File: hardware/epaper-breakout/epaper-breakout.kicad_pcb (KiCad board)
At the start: 2 copper layers, 88 x 67 mm, 107 parts, among them J1 USB_C_16P, J2 Conn_02x06_Counter_Clockwise, Q1 AO3401A, Q2 MMBT3904, Q3 MMBT3904, Q4 MMBT3904, Q5 2N7002, Q6 AO3401A, Q7 AO3401A, SW1 SW_DIP_x01, U1 LT1945, U10 ESP32-WROVER, U11 PCF8563T, U12 MCP9700AT-ETT, U13 ED060XC5, U14 FPC-TOUCH, U2 LT1945, U3 XC6206PxxxMR, U4 CH340C, U5 74HC4094-normal, U6 LM358, U7 CONN-Battery, U8 TP4056, U9 MCP1700-3302E_SOT23, Y1 Crystal

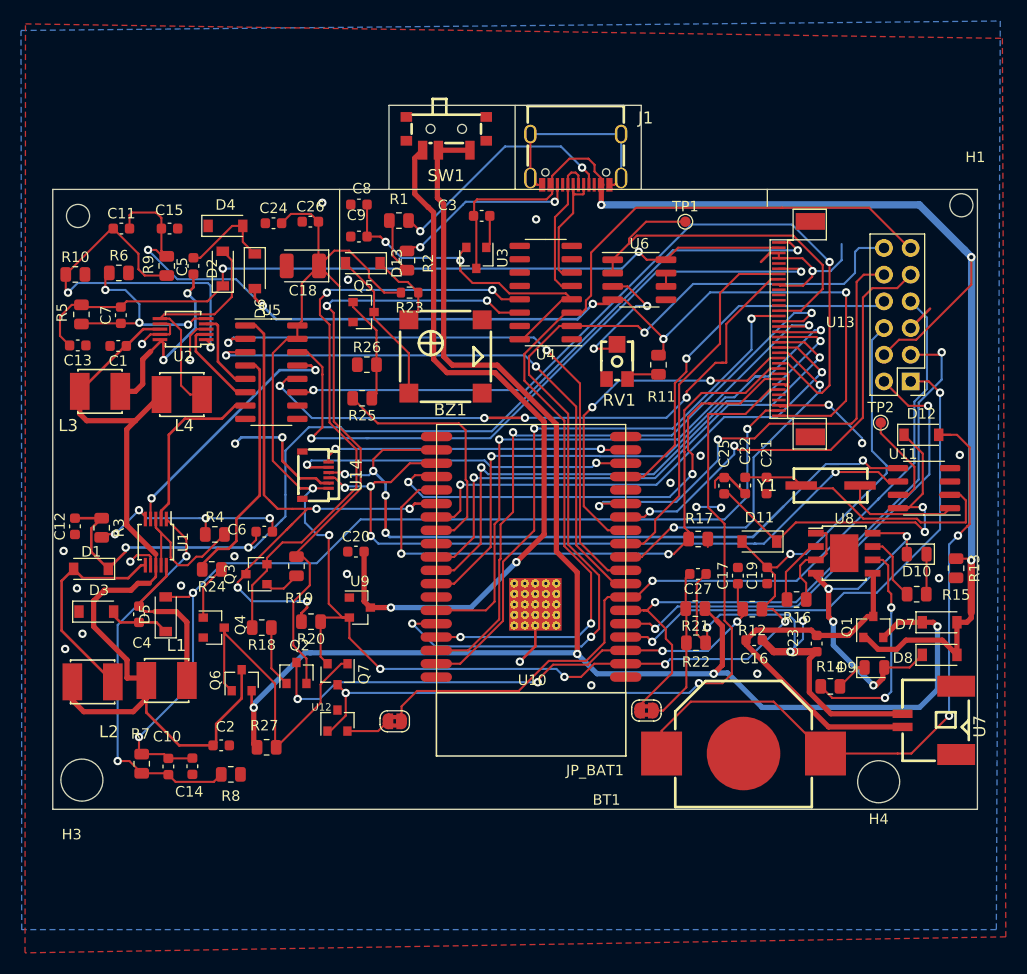
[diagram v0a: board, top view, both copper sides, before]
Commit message: change i2c bus pin
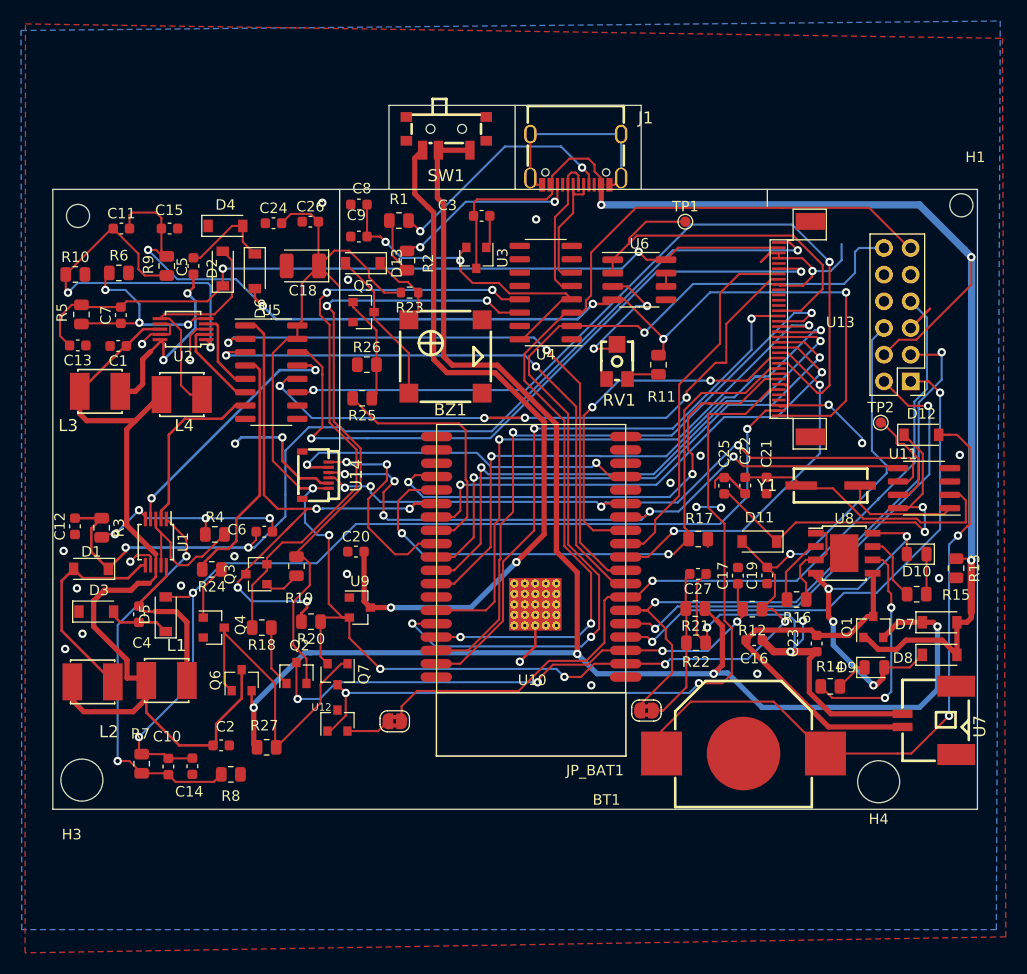
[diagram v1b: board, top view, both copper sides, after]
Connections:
- J1 pad A8: (no net) -> Net-(J1-PadA8)
- J1 pad B8: (no net) -> Net-(J1-PadB8)
- J2 pad 10: /MISO -> Net-(J2-Pad10)
- J2 pad 8: /MOSI -> Net-(J2-Pad8)
- J2 pad 9: /SCLK -> Net-(J2-Pad9)
- U10 pad 13: /SCLK -> /TCH_SDA
- U10 pad 14: /MISO -> /TCH_SCL
- U10 pad 16: /MOSI -> /TCH_INT
- U10 pad 17: /TCH_INT -> Net-(U10-Pad17)
- U10 pad 18: /TCH_RST -> Net-(U10-Pad18)
- U10 pad 19: (no net) -> Net-(U10-Pad19)
- U10 pad 20: (no net) -> Net-(U10-Pad20)
- U10 pad 21: /TCH_SDA -> Net-(U10-Pad21)
- U10 pad 22: /TCH_SCL -> Net-(U10-Pad22)
- U10 pad 28: (no net) -> /TCH_RST
- U10 pad 32: (no net) -> Net-(U10-Pad32)
- U11 pad 3: (no net) -> Net-(U11-Pad3)
- U13 pad 22: (no net) -> Net-(U13-Pad22)
- U13 pad 23: (no net) -> Net-(U13-Pad23)
- U13 pad 24: (no net) -> Net-(U13-Pad24)
- U13 pad 25: (no net) -> Net-(U13-Pad25)
- U13 pad 30: (no net) -> Net-(U13-Pad30)
- U13 pad 4: (no net) -> Net-(U13-Pad4)
- U13 pad 5: (no net) -> Net-(U13-Pad5)
- U4 pad 10: (no net) -> Net-(U4-Pad10)
- U4 pad 11: (no net) -> Net-(U4-Pad11)
- U4 pad 12: (no net) -> Net-(U4-Pad12)
- U4 pad 15: (no net) -> Net-(U4-Pad15)
- U4 pad 7: (no net) -> Net-(U4-Pad7)
- U4 pad 8: (no net) -> Net-(U4-Pad8)
- U4 pad 9: (no net) -> Net-(U4-Pad9)
- U5 pad 10: (no net) -> Net-(U5-Pad10)
- U5 pad 9: (no net) -> Net-(U5-Pad9)
- U8 pad 9: (no net) -> Net-(U8-Pad9)
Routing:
- net /MISO: track 47.7 -> 0.00 mm, vias 2 -> 0
- net /SCLK: track 44.2 -> 0.00 mm, vias 2 -> 0
- net /MOSI: track 35.7 -> 0.00 mm, vias 1 -> 0
- net /TCH_RST: track 29.6 -> 20.3 mm
- net /TCH_SDA: track 71.9 -> 65.0 mm
- net /TCH_SCL: track 72.2 -> 66.3 mm
- net /TCH_INT: track 33.3 -> 34.5 mm
- net /EP_STH: track 34.6 -> 35.5 mm
- net Net-(TP2-Pad1): track 9.41 -> 10.2 mm
- net Net-(J2-Pad8): track 0.00 -> 0.63 mm

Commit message: change usb-c type
2022-08-27
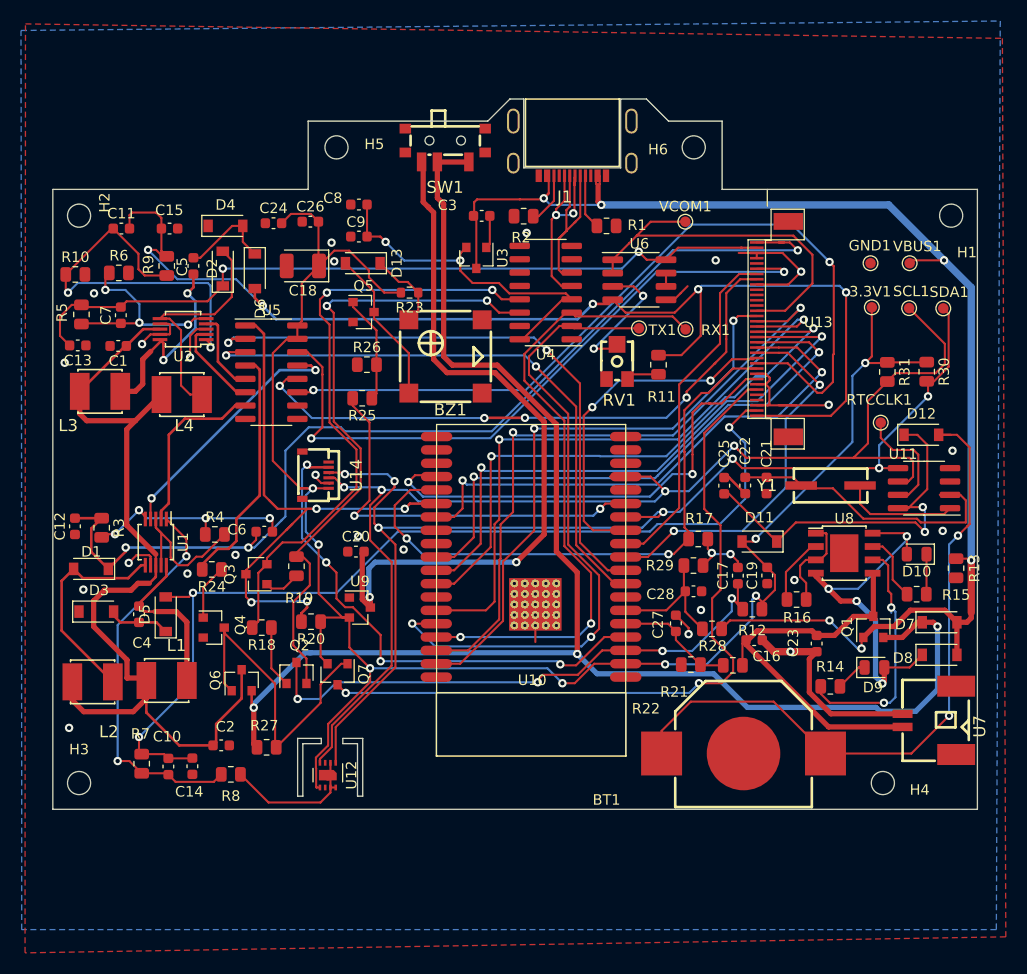
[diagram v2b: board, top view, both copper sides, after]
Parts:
- removed J2: Conn_02x06_Counter_Clockwise, Connector_PinHeader_2.54mm:PinHeader_2x06_P2.54mm_Vertical
- removed JP_BAT1, JP_TEMP1: Jumper, Jumper:SolderJumper-2_P1.3mm_Bridged2Bar_RoundedPad1.0x1.5mm
- added 3.3V1: TestPoint_Probe, TestPoint:TestPoint_Pad_D1.0mm, F.Cu at (101.0, 42.2)
- added C28: 0.1uF, Capacitor_SMD:C_0603_1608Metric, F.Cu at (84.0, 69.2)
- added GND1: TestPoint_Probe, TestPoint:TestPoint_Pad_D1.0mm, F.Cu at (100.8, 38.0)
- added H5: MountingHole, MountingHole:MountingHole_2.2mm_M2, F.Cu at (50.0, 27.0)
- added H6: MountingHole, MountingHole:MountingHole_2.2mm_M2, F.Cu at (84.0, 27.0)
- added R28: 680k, Resistor_SMD:R_0805_2012Metric, F.Cu at (85.7, 72.8)
- added R29: 150k, Resistor_SMD:R_0805_2012Metric, F.Cu at (84.0, 66.8)
- added R30: 10k, Resistor_SMD:R_0805_2012Metric, F.Cu at (106.2, 48.4)
- added R31: 10k, Resistor_SMD:R_0805_2012Metric, F.Cu at (102.4, 48.4)
- added RX1: TestPoint_Probe, TestPoint:TestPoint_Pad_D1.0mm, F.Cu at (83.2, 44.3)
- added SCL1: TestPoint_Probe, TestPoint:TestPoint_Pad_D1.0mm, F.Cu at (104.5, 42.3)
- added SDA1: TestPoint_Probe, TestPoint:TestPoint_Pad_D1.0mm, F.Cu at (107.8, 42.3)
- added TX1: TestPoint_Probe, TestPoint:TestPoint_Pad_D1.0mm, F.Cu at (78.8, 44.2)
- added VBUS1: TestPoint_Probe, TestPoint:TestPoint_Pad_D1.0mm, F.Cu at (104.5, 38.0)
- H3, H4: footprint MountingHole:MountingHole_4mm -> MountingHole:MountingHole_2.2mm_M2
- J1: footprint epaper-breakout:JLC_USB-C-SMD_KH-TYPE-C-16P -> epaper-breakout:JLC_USB-C-SMD_TYPE-C-31-M-13C
- U12: value MCP9700AT-ETT -> GHT30_DIS; footprint Package_TO_SOT_SMD:SOT-23 -> Sensor_Humidity:Sensirion_DFN-8-1EP_2.5x2.5mm_P0.5mm_EP1.1x1.7mm
- moved R1 19.8 mm to (75.7, 34.5), turned to 0 degrees
- moved R2 11.9 mm to (67.8, 33.5), turned to 180 degrees
- moved R21 6.48 mm to (87.7, 76.3)
- moved U12 5.28 mm to (49.2, 86.8), turned to 270 degrees
- moved C27 5.15 mm to (82.3, 72.3), turned to 270 degrees
- moved R22 2.13 mm to (83.7, 76.2), turned to 180 degrees
- moved U13 2.10 mm to (90.0, 44.3)
- moved H1 1.39 mm to (108.5, 33.5)
- moved SW1 1.12 mm to (60.4, 26.8)
- moved J1 1.10 mm to (72.5, 27.1)
- moved H4 0.42 mm to (102.0, 87.5)
- moved H3 0.39 mm to (25.5, 87.5)
- moved H2 0.10 mm to (25.5, 33.5), turned to 180 degrees
- renumbered TP2 to RTCCLK1, TP1 to VCOM1
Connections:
- C27 pad 2: Net-(C27-Pad2) -> /SENSOR_BAT
- R21 pad 1: VIN -> BAT+
- R21 pad 2: Net-(C27-Pad2) -> /SENSOR_BAT
- R22 pad 1: Net-(C27-Pad2) -> /SENSOR_BAT
- U10 pad 14: /TCH_SCL -> /BUZZER
- U10 pad 16: /TCH_INT -> /TCH_SCL
- U10 pad 27: /BUZZER -> Net-(U10-Pad27)
- U10 pad 28: /TCH_RST -> Net-(U10-Pad28)
- U10 pad 4: /SENSOR_VP -> /TCH_INT
- U10 pad 5: /SENSOR_VN -> /SENSOR_BAT
- U10 pad 6: /A0 -> /SENSOR_VBUS
- U10 pad 7: /A1 -> Net-(U10-Pad7)
- U12 pad 1: EPD_VDD -> /TCH_SDA
- U12 pad 2: Net-(JP_TEMP1-Pad1) -> GND
- U12 pad 3: GND -> Net-(U12-Pad3)
- U14 pad 6: /TCH_RST -> Net-(U14-Pad6)
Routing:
- net /A1: track 78.9 -> 0.00 mm, vias 1 -> 0
- net /A0: track 61.4 -> 0.00 mm, vias 2 -> 0
- net /TCH_SCL: track 66.3 -> 120.9 mm
- net /SENSOR_VP: track 50.9 -> 0.00 mm, vias 2 -> 0
- net GND: track 168.1 -> 119.4 mm, vias 30 -> 26
- net /TCH_SDA: track 65.0 -> 112.5 mm, vias 5 -> 7
- net /SENSOR_VN: track 46.9 -> 0.00 mm, vias 2 -> 0
- net /USB_RXD: track 91.5 -> 62.1 mm
- net /USB_TXD: track 90.2 -> 62.1 mm, vias 3 -> 2
- net /TCH_RST: track 20.3 -> 0.00 mm, vias 2 -> 0
- net Net-(J1-PadA5): track 23.0 -> 5.25 mm, vias 2 -> 0
- net Net-(C27-Pad2): track 15.0 -> 0.00 mm
- net /TCH_INT: track 34.5 -> 49.5 mm, vias 2 -> 4
- net /BUZZER: track 23.8 -> 38.7 mm, vias 0 -> 2
- net /+3.3V: track 161.1 -> 174.5 mm, vias 7 -> 8
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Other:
- board size 88 x 67 mm -> 88 x 67.6 mm

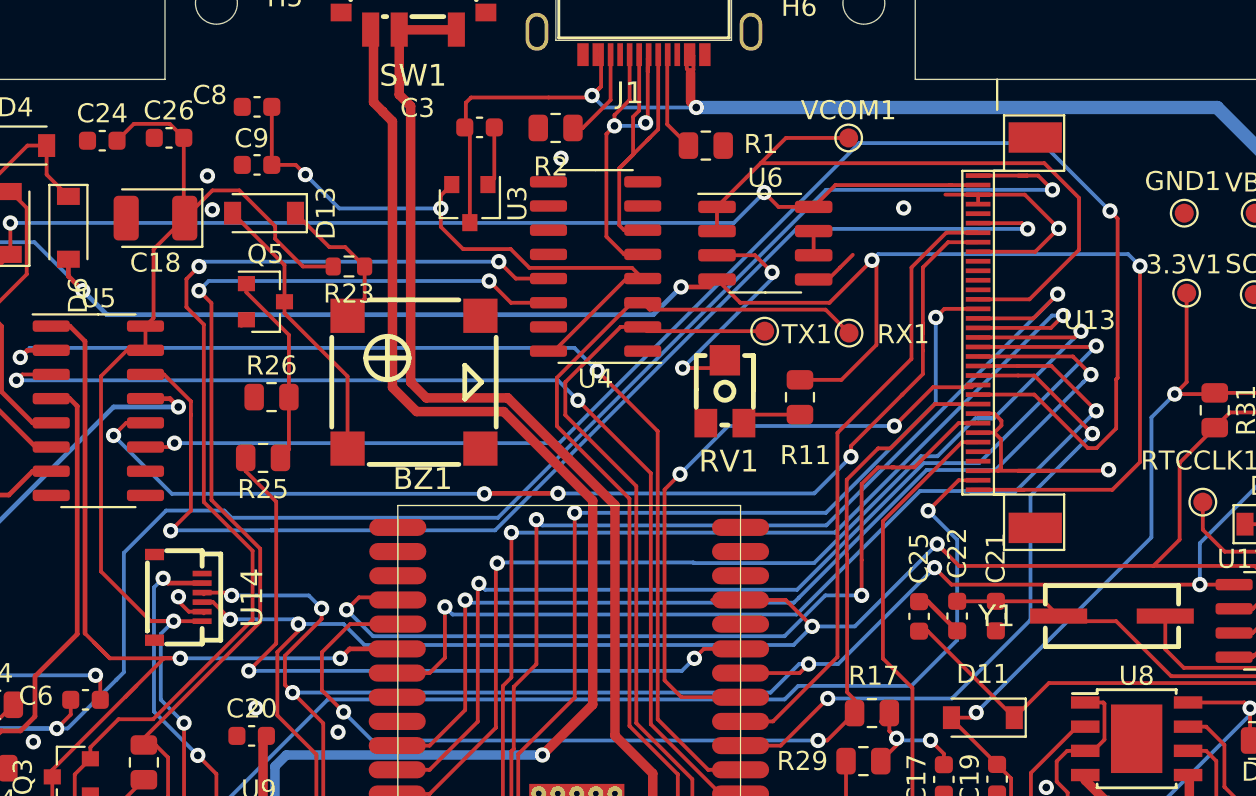
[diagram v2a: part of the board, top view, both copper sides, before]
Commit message: change FPC connector
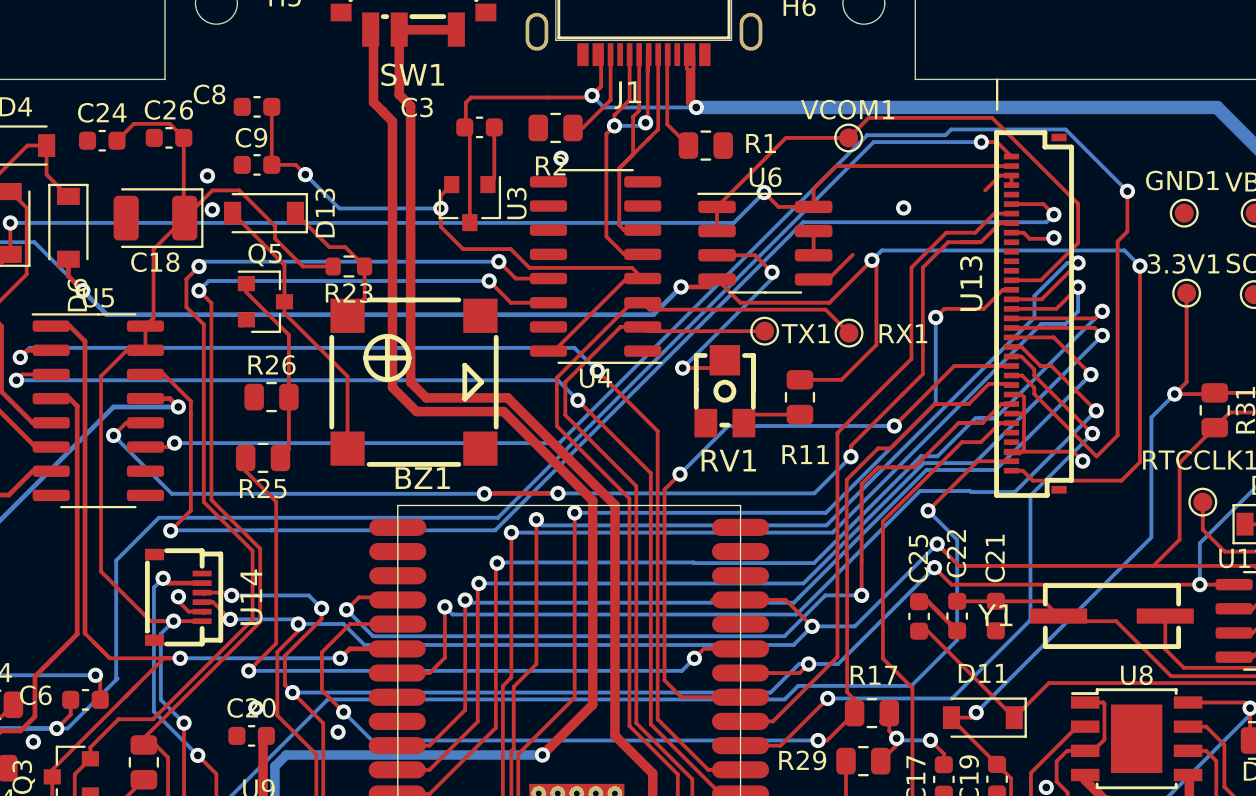
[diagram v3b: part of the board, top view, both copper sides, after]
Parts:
- U13: footprint epaper-breakout:X05A20H34G -> epaper-breakout:JLC_FFC-SMD_34P-P0.50_FH34SRJ-34S-0.5SH
- moved U13 3.16 mm to (93.0, 43.3)
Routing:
- net GND: track 119.4 -> 108.0 mm
- net /EP_VCOM: track 36.3 -> 30.4 mm
- net /+22V: track 97.4 -> 91.6 mm
- net /EP_CKH: track 44.9 -> 48.1 mm
- net /EP_MODE: track 58.3 -> 61.4 mm
- net /15V: track 74.0 -> 76.6 mm
- net /-15V: track 113.6 -> 111.4 mm
- net /EP_LE: track 57.2 -> 59.4 mm
- net /-20V: track 92.3 -> 94.5 mm
- net EPD_VDD: track 70.0 -> 72.2 mm
- net /EP_STH: track 33.4 -> 35.5 mm
- net /EP_D7: track 55.8 -> 58.0 mm
- net /EP_CKV: track 32.8 -> 35.0 mm
- net /EP_D6: track 62.8 -> 64.8 mm
- net /EP_OE: track 79.2 -> 80.8 mm
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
